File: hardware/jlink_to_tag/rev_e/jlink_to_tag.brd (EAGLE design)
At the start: 31.5 x 33 mm, 14 parts, among them J2 JLINK_6PIN_TAG-CON, U1 LT1763CS8-3.3

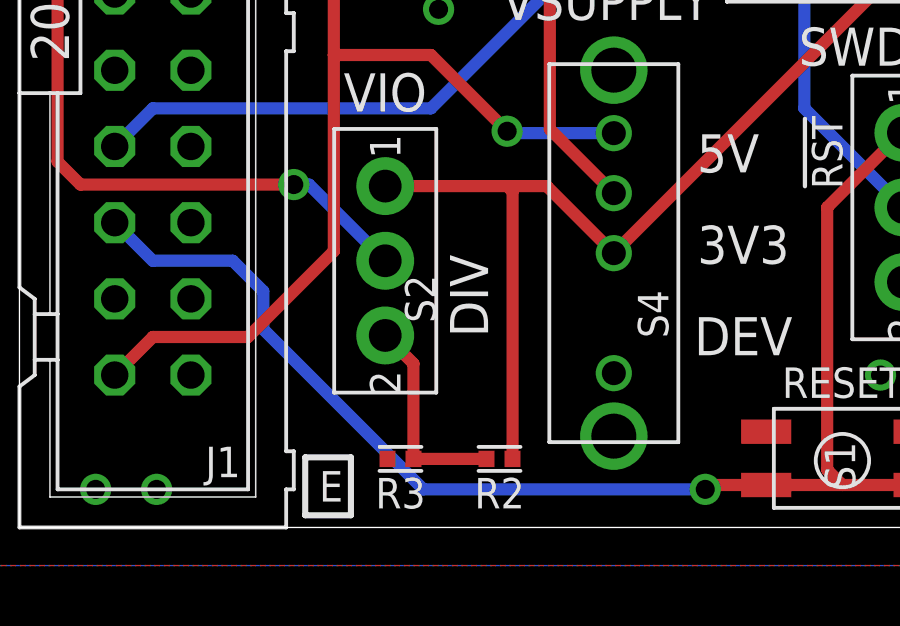
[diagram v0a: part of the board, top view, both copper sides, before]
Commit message: update part numbers
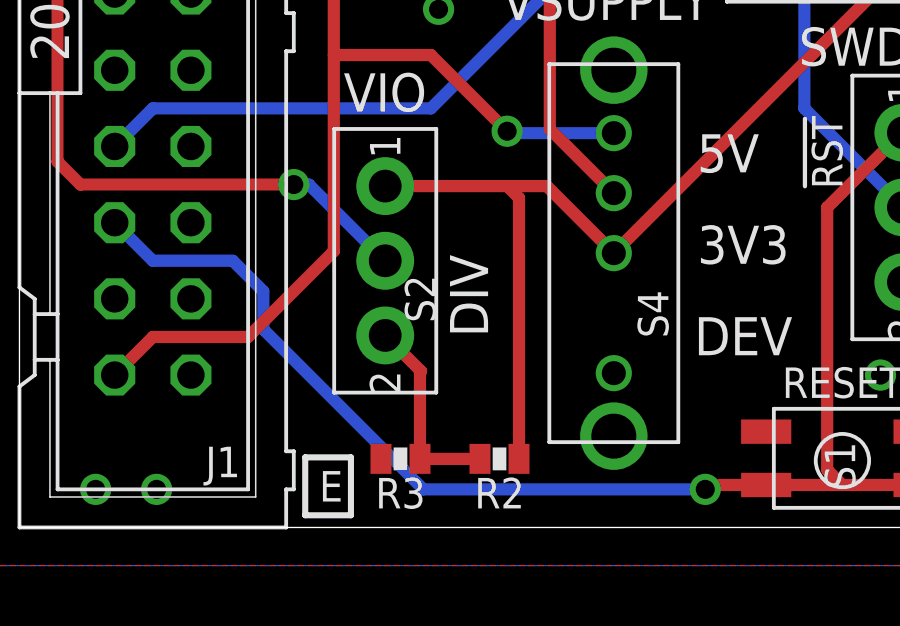
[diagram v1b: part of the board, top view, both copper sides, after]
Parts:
- R2, R3: device passives:0402_RES -> passives:0603-RES
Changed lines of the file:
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@@
 </element>
 <element name="S2" library="switches" package="TE_SSA12/SPDT" value="TE_SSA12/SPDT" x="12.192" y="8.89" smashed="yes" rot="R270">
-<attribute name="DIGIKEY" value="450-1602-ND" x="12.192" y="8.89" size="1.778" layer="27" rot="R270" display="off"/>
+<attribute name="DIGIKEY" value="2223-SLW-883935-2A-D-ND" x="12.192" y="8.89" size="1.778" layer="27" rot="R270" display="off"/>
+<attribute name="MPN" value="SLW-883935-2A-D" x="12.192" y="8.89" size="1.778" layer="27" rot="R270" display="off"/>
 <attribute name="NAME" x="13.8684" y="7.62" size="1.016" layer="25" font="vector" ratio="12" rot="R90" align="bottom-center"/>
 <attribute name="VALUE" x="9.017" y="8.89" size="1.016" layer="27" font="vector" ratio="12" rot="R270" align="bottom-center"/>
 </element>
 <element name="S3" library="switches" package="TE_SSA12/SPDT" value="TE_SSA12/SPDT" x="29.464" y="10.668" smashed="yes" rot="R270">
-<attribute name="DIGIKEY" value="450-1602-ND" x="29.464" y="10.668" size="1.778" layer="27" rot="R270" display="off"/>
+<attribute name="DIGIKEY" value="2223-SLW-883935-2A-D-ND" x="29.464" y="10.668" size="1.778" layer="27" rot="R270" display="off"/>
+<attribute name="MPN" value="SLW-883935-2A-D" x="29.464" y="10.668" size="1.778" layer="27" rot="R270" display="off"/>
 <attribute name="NAME" x="30.099" y="9.652" size="1.016" layer="25" font="vector" ratio="12" rot="R270" align="bottom-center"/>
 <attribute name="VALUE" x="26.289" y="10.668" size="1.016" layer="27" font="vector" ratio="12" rot="R270" align="bottom-center"/>
@@
 <attribute name="NAME" x="21.63" y="7.112" size="1.016" layer="25" font="vector" ratio="12" rot="R90" align="bottom-center"/>
 </element>
-<element name="R2" library="passives" package="0402_RES" value="10k" x="16.002" y="2.286" smashed="yes">
+<element name="R2" library="passives" package="0603-RES" value="10k" x="16.002" y="2.286" smashed="yes">
 <attribute name="NAME" x="16.002" y="0.635" size="1.016" layer="25" font="vector" ratio="12" align="bottom-center"/>
 <attribute name="VALUE" x="16.002" y="0.889" size="1.016" layer="27" font="vector" ratio="12" align="bottom-center"/>
 </element>
-<element name="R3" library="passives" package="0402_RES" value="20k" x="12.7" y="2.286" smashed="yes">
+<element name="R3" library="passives" package="0603-RES" value="20k" x="12.7" y="2.286" smashed="yes">
 <attribute name="NAME" x="12.7" y="0.635" size="1.016" layer="25" font="vector" ratio="12" align="bottom-center"/>
 <attribute name="VALUE" x="12.7" y="0.889" size="1.016" layer="27" font="vector" ratio="12" align="bottom-center"/>
@@
 <contactref element="R3" pad="1"/>
 <via x="28.702" y="5.08" extent="1-16" drill="0.635"/>
+<wire x1="19.812" y1="30.734" x2="28.702" y2="27.686" width="0" layer="19" extent="1-1"/>
+<wire x1="15.681" y1="26.6446" x2="19.812" y2="30.734" width="0" layer="19" extent="1-1"/>
+<wire x1="10.481" y1="26.6446" x2="15.681" y2="26.6446" width="0" layer="19" extent="1-1"/>
+<wire x1="10.481" y1="25.3746" x2="10.481" y2="26.6446" width="0" layer="19" extent="1-1"/>
+<wire x1="10.4872" y1="30.0736" x2="10.481" y2="26.6446" width="0" layer="19" extent="1-1"/>
+<wire x1="12.1784" y1="21.5646" x2="10.481" y2="25.3746" width="0" layer="19" extent="1-1"/>
+<wire x1="14.4272" y1="21.2986" x2="12.1784" y2="21.5646" width="0" layer="19" extent="1-1"/>
+<wire x1="13.97" y1="17.272" x2="14.4272" y2="21.2986" width="0" layer="19" extent="1-1"/>
+<wire x1="5.715" y1="25.4" x2="10.481" y2="25.3746" width="0" layer="19" extent="1-1"/>
+<wire x1="5.715" y1="22.86" x2="5.715" y2="25.4" width="0" layer="19" extent="1-1"/>
+<wire x1="5.715" y1="20.32" x2="5.715" y2="22.86" width="0" layer="19" extent="1-1"/>
+<wire x1="5.715" y1="17.78" x2="5.715" y2="20.32" width="0" layer="19" extent="1-1"/>
+<wire x1="5.715" y1="15.24" x2="5.715" y2="17.78" width="0" layer="19" extent="1-1"/>
+<wire x1="5.715" y1="12.7" x2="5.715" y2="15.24" width="0" layer="19" extent="1-1"/>
+<wire x1="5.715" y1="10.16" x2="5.715" y2="12.7" width="0" layer="19" extent="1-1"/>
+<wire x1="5.715" y1="7.62" x2="5.715" y2="10.16" width="0" layer="19" extent="1-1"/>
+<wire x1="5.715" y1="5.08" x2="5.715" y2="7.62" width="0" layer="19" extent="1-1"/>
+<wire x1="4.572" y1="1.27" x2="5.715" y2="5.08" width="0" layer="19" extent="1-1"/>
+<wire x1="2.54" y1="1.27" x2="4.572" y2="1.27" width="0" layer="19" extent="1-1"/>
+<wire x1="2.286" y1="30.988" x2="5.715" y2="25.4" width="0" layer="19" extent="1-1"/>
+<wire x1="12.05" y1="2.286" x2="5.715" y2="5.08" width="0" layer="19" extent="1-1"/>
+<wire x1="24.892" y1="3.194" x2="12.05" y2="2.286" width="0" layer="19" extent="1-1"/>
+<wire x1="28.702" y1="5.08" x2="24.892" y2="3.194" width="0" layer="19" extent="1-1"/>
+<wire x1="29.972" y1="3.194" x2="28.702" y2="5.08" width="0" layer="19" extent="1-1"/>
 </signal>
 <signal name="NRESET">
@@
 <wire x1="16.256" y1="11.3792" x2="17.5768" y2="11.3792" width="0.4064" layer="1"/>
 <wire x1="17.5768" y1="11.3792" x2="19.812" y2="9.144" width="0.4064" layer="1"/>
-<wire x1="16.43506875" y1="2.286" x2="16.43506875" y2="11.20013125" width="0.4064" layer="1"/>
-<wire x1="16.43506875" y1="11.20013125" x2="16.256" y2="11.3792" width="0.4064" layer="1"/>
+<wire x1="16.652" y1="2.286" x2="16.652" y2="10.9832" width="0.4064" layer="1"/>
+<wire x1="16.652" y1="10.9832" x2="16.256" y2="11.3792" width="0.4064" layer="1"/>
 </signal>
 <signal name="N$1">
@@
 <contactref element="R2" pad="1"/>
 <contactref element="S2" pad="2"/>
-<wire x1="12.192" y1="6.4008" x2="13.13306875" y2="5.45973125" width="0.4064" layer="1"/>
-<wire x1="13.13306875" y1="5.45973125" x2="13.13306875" y2="2.286" width="0.4064" layer="1"/>
-<wire x1="13.13306875" y1="2.286" x2="15.56893125" y2="2.286" width="0.4064" layer="1"/>
+<wire x1="12.192" y1="6.4008" x2="13.38706875" y2="5.20573125" width="0.4064" layer="1"/>
+<wire x1="13.38706875" y1="5.20573125" x2="13.35" y2="5.203196875" width="0.4064" layer="1"/>
+<wire x1="13.35" y1="5.203196875" x2="13.35" y2="2.286" width="0.4064" layer="1"/>
+<wire x1="13.35" y1="2.286" x2="15.352" y2="2.286" width="0.4064" layer="1"/>
 </signal>
 </signals>

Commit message: add BOM and final changes
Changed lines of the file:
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@@
 </element>
 <element name="D1" library="SparkFun-LED" package="LED-0603" value="BLUE" x="14.4272" y="20.4216" smashed="yes">
+<attribute name="DIGIKEY" value="160-1827-1-ND" x="14.4272" y="20.4216" size="1.778" layer="27" display="off"/>
 <attribute name="NAME" x="13.8557" y="20.9296" size="1.016" layer="25" font="vector" ratio="12" rot="R90" align="bottom-center"/>
 <attribute name="PROD_ID" value="DIO-08575" x="14.4272" y="20.4216" size="1.016" layer="27" ratio="12" display="off"/>
@@
 </element>
 <element name="R1" library="SparkFun-Passives" package="0603-RES" value="470" x="11.3284" y="19.5326" smashed="yes">
+<attribute name="DIGIKEY" value="P470DBCT-ND" x="11.3284" y="19.5326" size="1.778" layer="27" display="off"/>
 <attribute name="NAME" x="11.3284" y="18.9738" size="1.016" layer="25" font="vector" ratio="12" rot="R180" align="bottom-center"/>
 <attribute name="VALUE" x="10.3124" y="18.3896" size="0.4064" layer="27" font="vector"/>
@@
 </element>
 <element name="R2" library="passives" package="0603-RES" value="10k" x="16.002" y="2.286" smashed="yes">
+<attribute name="DIGIKEY" value="RMCF0603FT10K0CT-ND" x="16.002" y="2.286" size="1.778" layer="27" display="off"/>
 <attribute name="NAME" x="16.002" y="0.635" size="1.016" layer="25" font="vector" ratio="12" align="bottom-center"/>
 <attribute name="VALUE" x="16.002" y="0.889" size="1.016" layer="27" font="vector" ratio="12" align="bottom-center"/>
 </element>
 <element name="R3" library="passives" package="0603-RES" value="20k" x="12.7" y="2.286" smashed="yes">
+<attribute name="DIGIKEY" value="P20.0KHCT-ND" x="12.7" y="2.286" size="1.778" layer="27" display="off"/>
 <attribute name="NAME" x="12.7" y="0.635" size="1.016" layer="25" font="vector" ratio="12" align="bottom-center"/>
 <attribute name="VALUE" x="12.7" y="0.889" size="1.016" layer="27" font="vector" ratio="12" align="bottom-center"/>
@@
 <contactref element="R3" pad="1"/>
 <via x="28.702" y="5.08" extent="1-16" drill="0.635"/>
-<wire x1="19.812" y1="30.734" x2="28.702" y2="27.686" width="0" layer="19" extent="1-1"/>
-<wire x1="15.681" y1="26.6446" x2="19.812" y2="30.734" width="0" layer="19" extent="1-1"/>
-<wire x1="10.481" y1="26.6446" x2="15.681" y2="26.6446" width="0" layer="19" extent="1-1"/>
-<wire x1="10.481" y1="25.3746" x2="10.481" y2="26.6446" width="0" layer="19" extent="1-1"/>
-<wire x1="10.4872" y1="30.0736" x2="10.481" y2="26.6446" width="0" layer="19" extent="1-1"/>
-<wire x1="12.1784" y1="21.5646" x2="10.481" y2="25.3746" width="0" layer="19" extent="1-1"/>
-<wire x1="14.4272" y1="21.2986" x2="12.1784" y2="21.5646" width="0" layer="19" extent="1-1"/>
-<wire x1="13.97" y1="17.272" x2="14.4272" y2="21.2986" width="0" layer="19" extent="1-1"/>
-<wire x1="5.715" y1="25.4" x2="10.481" y2="25.3746" width="0" layer="19" extent="1-1"/>
-<wire x1="5.715" y1="22.86" x2="5.715" y2="25.4" width="0" layer="19" extent="1-1"/>
-<wire x1="5.715" y1="20.32" x2="5.715" y2="22.86" width="0" layer="19" extent="1-1"/>
-<wire x1="5.715" y1="17.78" x2="5.715" y2="20.32" width="0" layer="19" extent="1-1"/>
-<wire x1="5.715" y1="15.24" x2="5.715" y2="17.78" width="0" layer="19" extent="1-1"/>
-<wire x1="5.715" y1="12.7" x2="5.715" y2="15.24" width="0" layer="19" extent="1-1"/>
-<wire x1="5.715" y1="10.16" x2="5.715" y2="12.7" width="0" layer="19" extent="1-1"/>
-<wire x1="5.715" y1="7.62" x2="5.715" y2="10.16" width="0" layer="19" extent="1-1"/>
-<wire x1="5.715" y1="5.08" x2="5.715" y2="7.62" width="0" layer="19" extent="1-1"/>
-<wire x1="4.572" y1="1.27" x2="5.715" y2="5.08" width="0" layer="19" extent="1-1"/>
-<wire x1="2.54" y1="1.27" x2="4.572" y2="1.27" width="0" layer="19" extent="1-1"/>
-<wire x1="2.286" y1="30.988" x2="5.715" y2="25.4" width="0" layer="19" extent="1-1"/>
-<wire x1="12.05" y1="2.286" x2="5.715" y2="5.08" width="0" layer="19" extent="1-1"/>
-<wire x1="24.892" y1="3.194" x2="12.05" y2="2.286" width="0" layer="19" extent="1-1"/>
-<wire x1="28.702" y1="5.08" x2="24.892" y2="3.194" width="0" layer="19" extent="1-1"/>
-<wire x1="29.972" y1="3.194" x2="28.702" y2="5.08" width="0" layer="19" extent="1-1"/>
 </signal>
 <signal name="NRESET">
@@
 <signal name="N$3">
 <contactref element="D1" pad="A"/>
-<wire x1="14.4138" y1="19.558" x2="14.4272" y2="19.5446" width="0.4064" layer="1"/>
 <contactref element="R1" pad="2"/>
 <wire x1="12.1784" y1="19.5326" x2="12.1904" y2="19.5446" width="0.4064" layer="1"/>
